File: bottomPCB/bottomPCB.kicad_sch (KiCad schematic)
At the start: 43 parts, among them J1 Conn_01x03_Pin, J2 Conn_02x03_Odd_Even, J3 Conn_01x02, J4 Conn_02x03_Odd_Even, U1 ESP32-WROOM-32, U2 XT30_horizontal, U3 XT30_horizontal, U8 LM1117IMPX-3_3_NOPB, U9 LM1117IMPX-3_3_NOPB

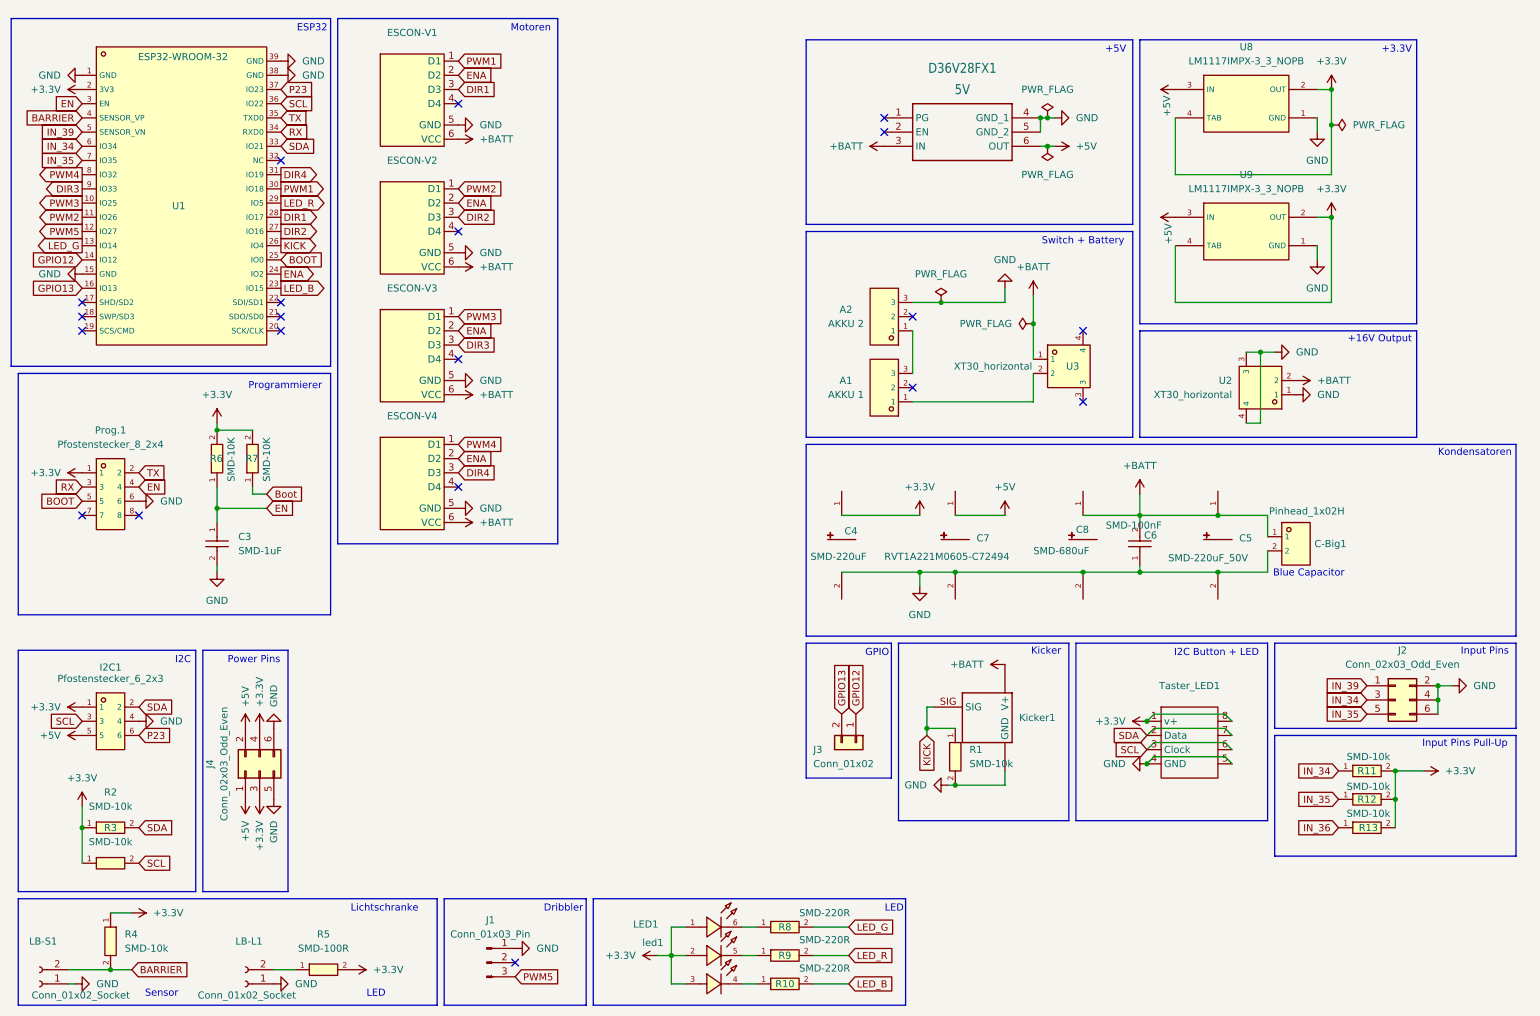
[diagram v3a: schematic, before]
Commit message: rearranged for vertical motor drivers
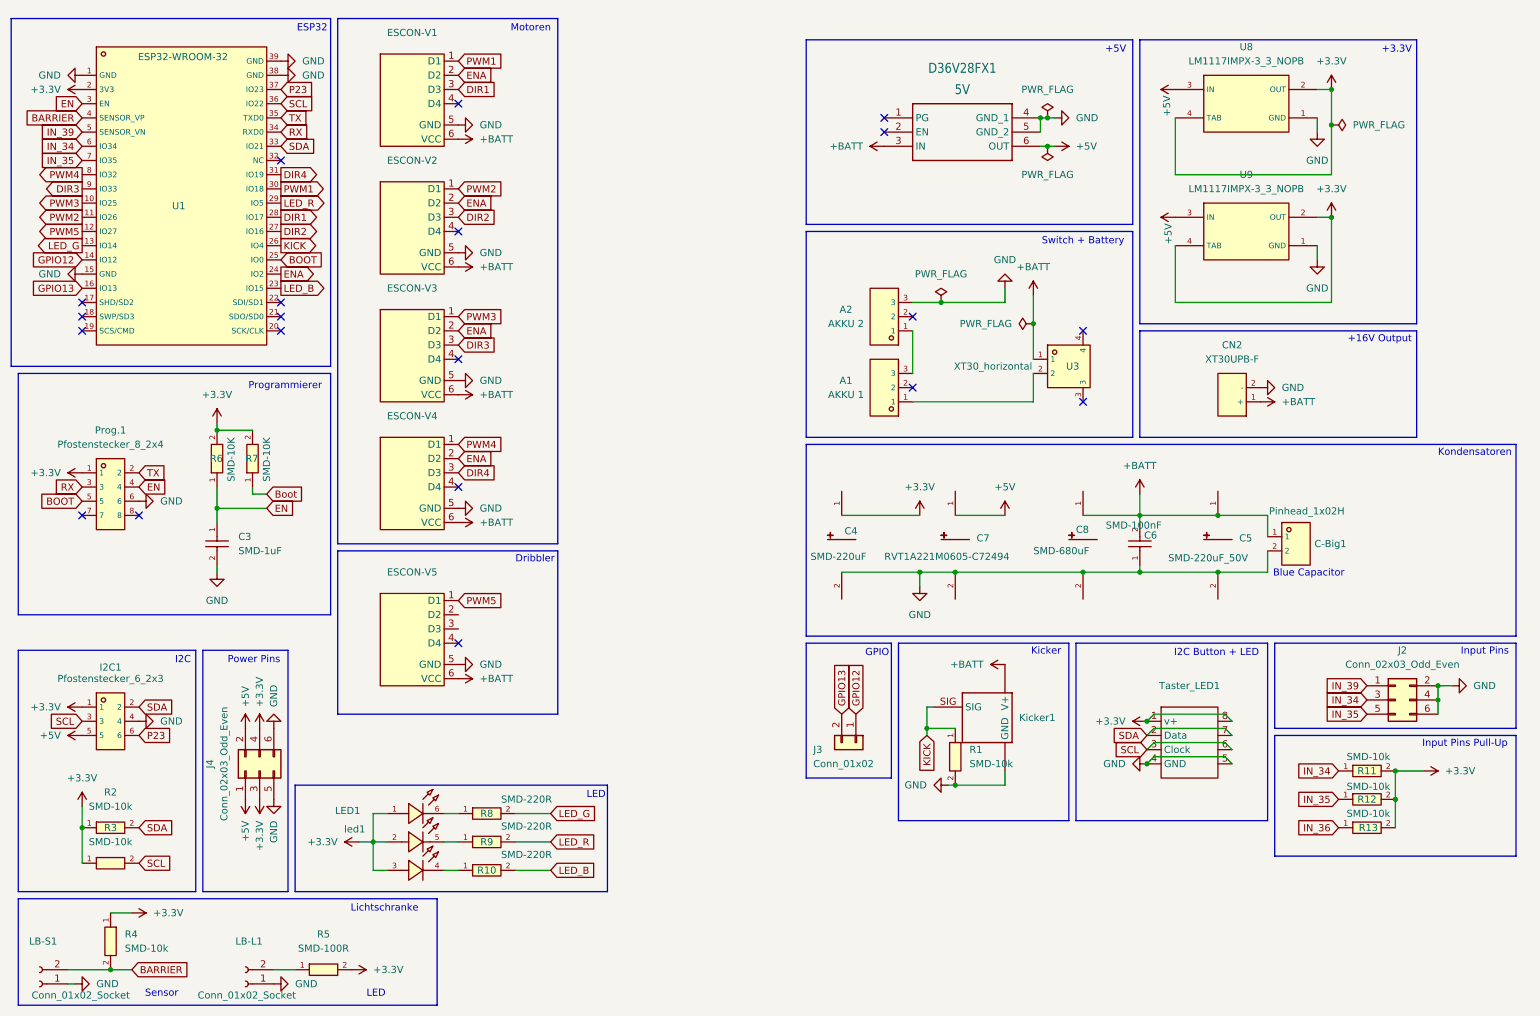
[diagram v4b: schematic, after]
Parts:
- removed J1: Conn_01x03_Pin, Connector_PinSocket_2.54mm:PinSocket_1x03_P2.54mm_Vertical, symbol Connector:Conn_01x03_Pin
- removed U2: XT30_horizontal, BohleBots:CONN-TH_XT30PW-M, symbol bohlebots.lib:XT30_horizontal
- added CN2: XT30UPB-F, BohleBots:CONN-TH_XT30UPB-F, symbol bohlebots.lib:XT30UPB-F
- added ESCON-V5: ~, sarcat:ESCON-V, symbol sarcat:ESCON-V
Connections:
- net +BATT: now also CN2.1 (+), ESCON-V5.6 (VCC)
- net GND: now also CN2.2 (-), ESCON-V5.5 (GND)
- net PWM5: now also ESCON-V5.1 (D1)
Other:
- moved on the sheet: LED1, R10, R8, R9

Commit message: added rules + changed layout
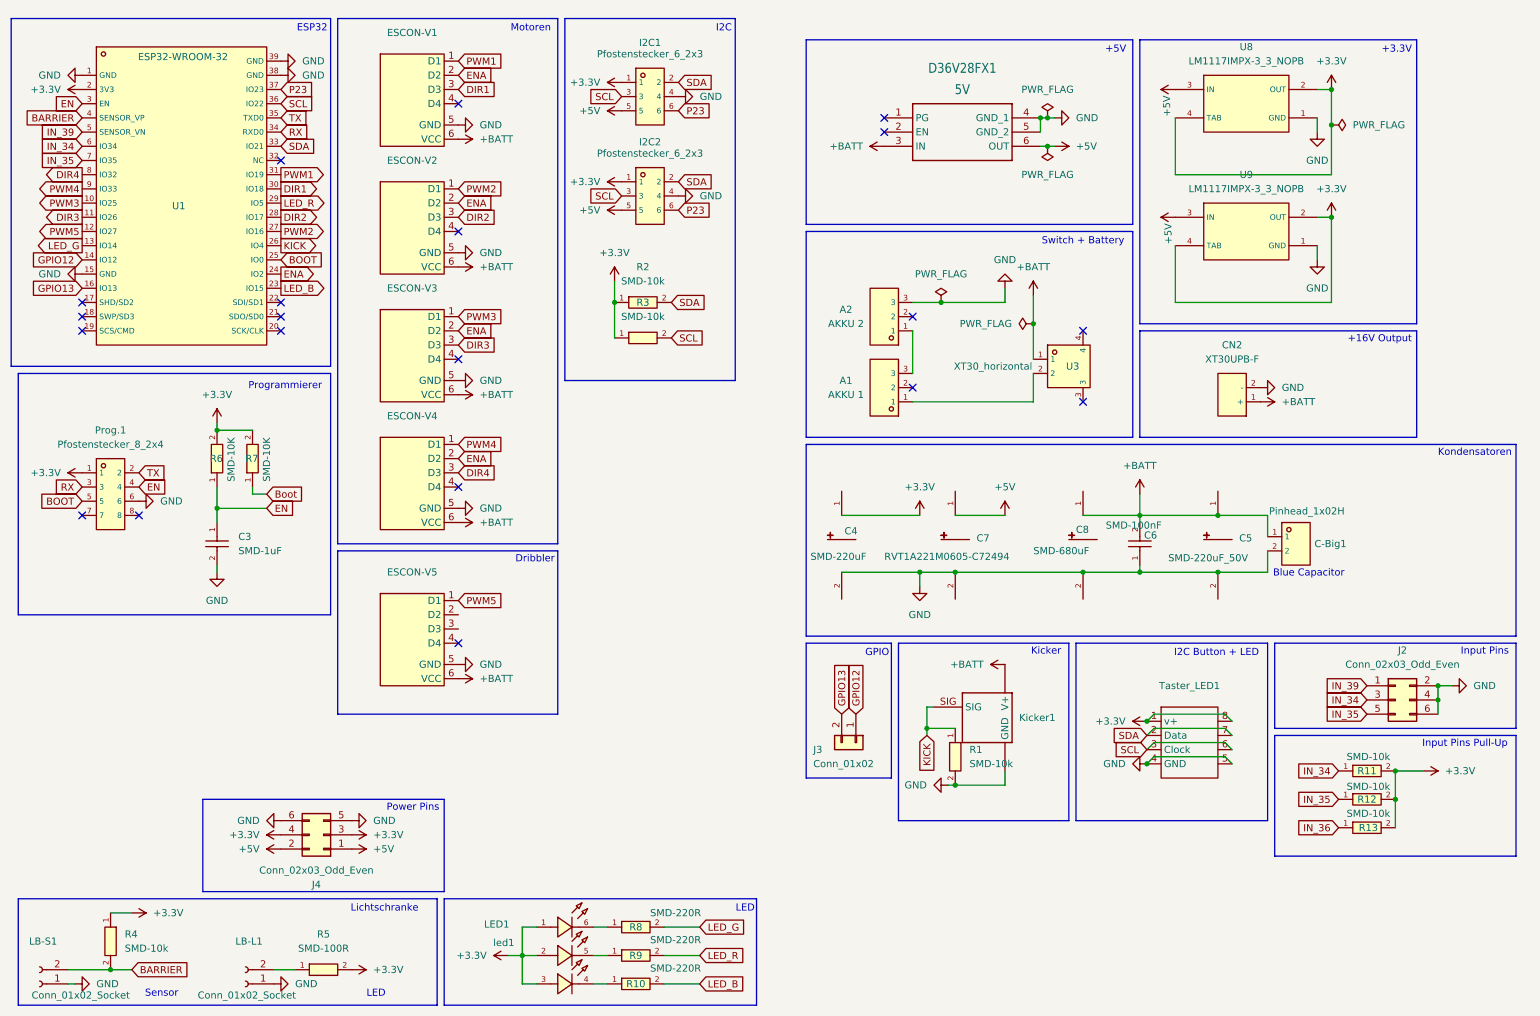
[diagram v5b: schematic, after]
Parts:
- added I2C2: Pfostenstecker_6_2x3, BohleBots:HDR-TH_6P-P2.54-V-F-R2-C3-S2.54-4, symbol bohlebots.lib:Pfostenstecker_6_2x3
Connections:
- net +3.3V: now also I2C2.1
- net +5V: now also I2C2.5
- net DIR1: now also U1.30 (IO18); no longer U1.28 (IO17)
- net DIR2: now also U1.28 (IO17); no longer U1.27 (IO16)
- net DIR3: now also U1.11 (IO26); no longer U1.9 (IO33)
- net DIR4: now also U1.8 (IO32); no longer U1.31 (IO19)
- net GND: now also I2C2.4
- net P23: now also I2C2.6
- net PWM1: now also U1.31 (IO19); no longer U1.30 (IO18)
- net PWM2: now also U1.27 (IO16); no longer U1.11 (IO26)
- net PWM4: now also U1.9 (IO33); no longer U1.8 (IO32)
- net SCL: now also I2C2.3
- net SDA: now also I2C2.2
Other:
- moved on the sheet: I2C1, J4, LED1, R10, R2, R3, R8, R9

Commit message: set traces
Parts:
- added H1, H2, H3, H4: MountingHole, BohleBots:MountingHole_4.3mm_M4, symbol bohlebots.lib:MountingHole
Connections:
- net Boot is gone; now on net BOOT: R7.1
- net IN_36 is gone; now on net IN_39: R13.1
- net +3.3V: now also ESCON-V5.2 (D2), ESCON-V5.3 (D3)
- net DIR2: now also U1.27 (IO16); no longer U1.28 (IO17)
- net DIR4: now also U1.9 (IO33); no longer U1.8 (IO32)
- net PWM2: now also U1.28 (IO17); no longer U1.27 (IO16)
- net PWM4: now also U1.8 (IO32); no longer U1.9 (IO33)

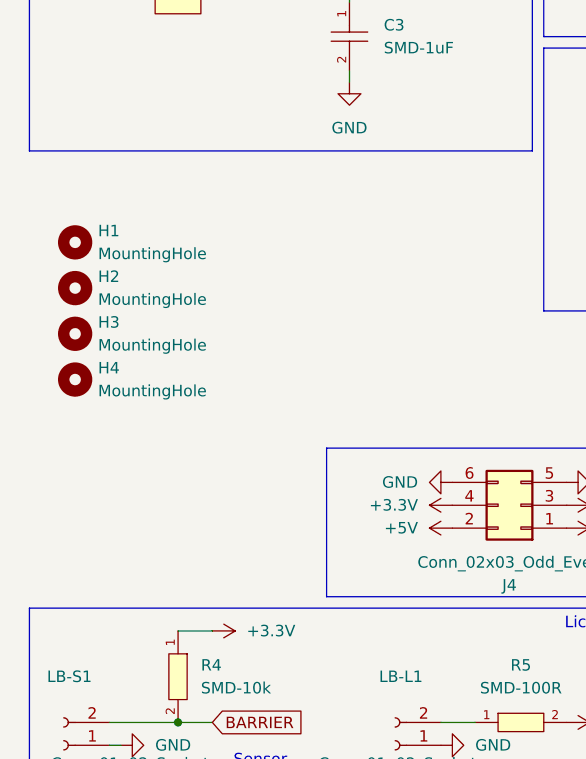
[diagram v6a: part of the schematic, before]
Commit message: Grounded Mounting Holes
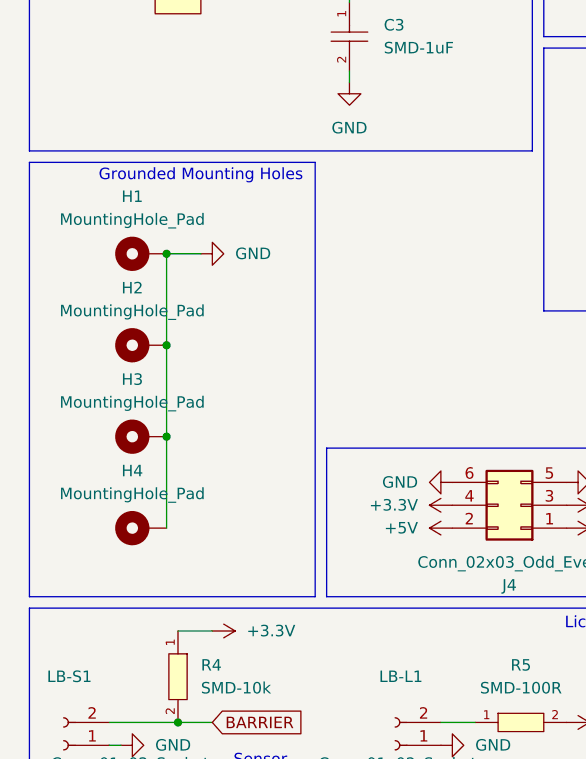
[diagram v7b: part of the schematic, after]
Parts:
- removed H1, H2, H3, H4: MountingHole, BohleBots:MountingHole_4.3mm_M4, symbol bohlebots.lib:MountingHole
- added H1, H2, H3, H4: MountingHole_Pad, MountingHole:MountingHole_4.3mm_M4_Pad, symbol Mechanical:MountingHole_Pad
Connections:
- net GND: now also H1.1, H2.1, H3.1, H4.1
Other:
- note added: "Grounded Mounting Holes"

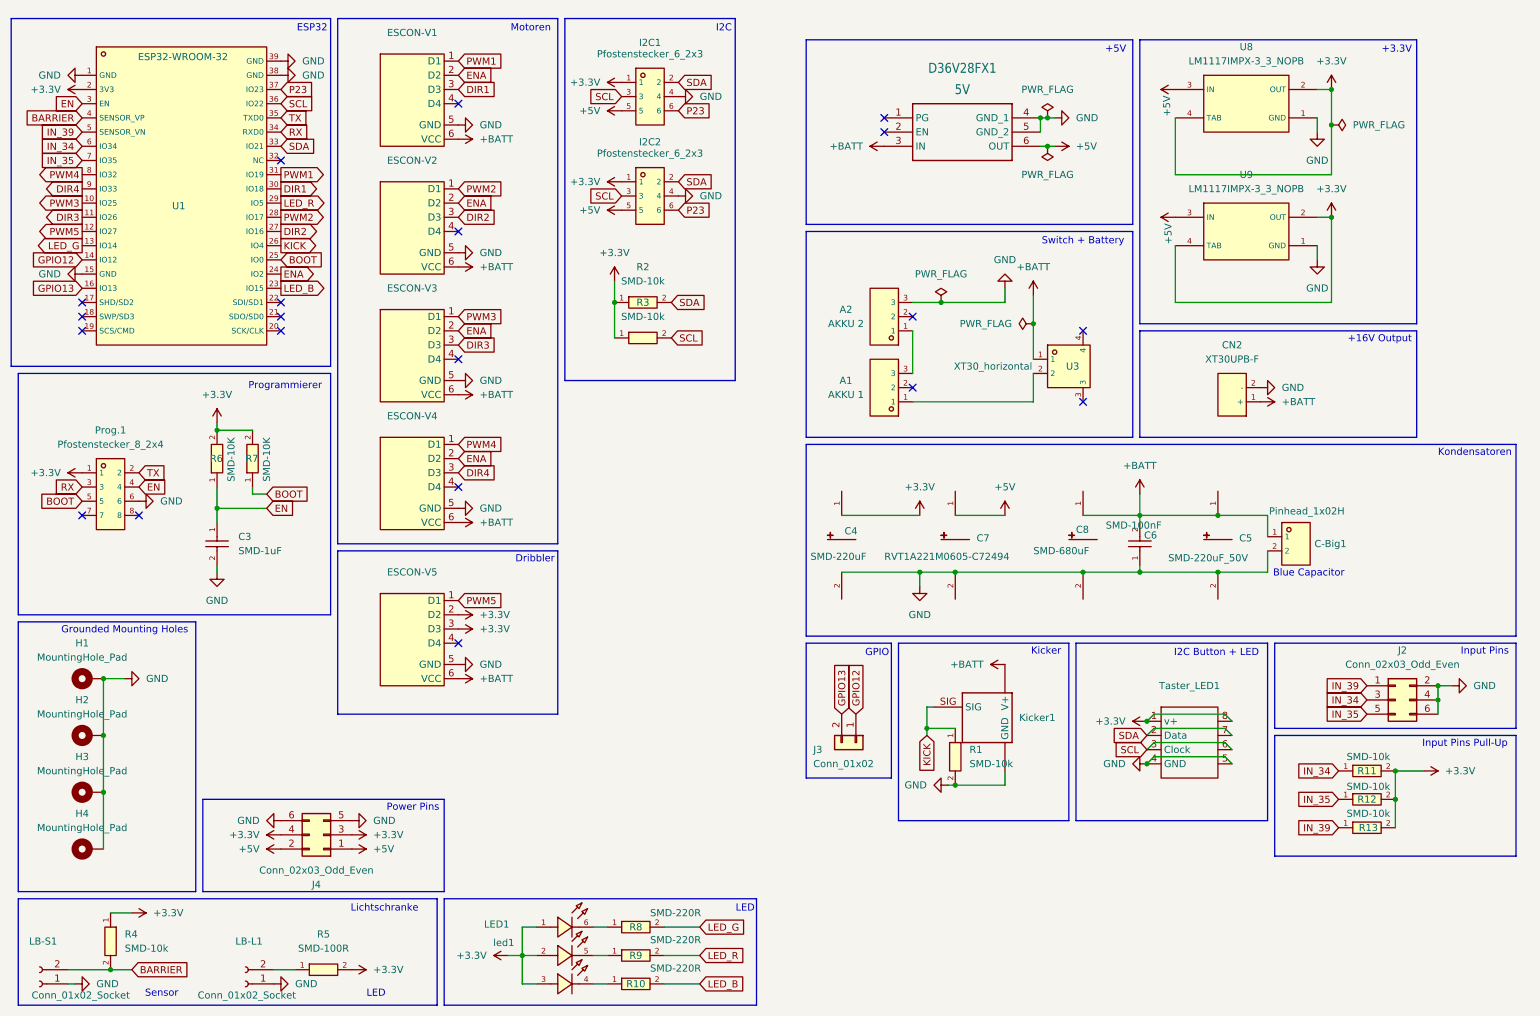
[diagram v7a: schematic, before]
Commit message: fixed erc errors
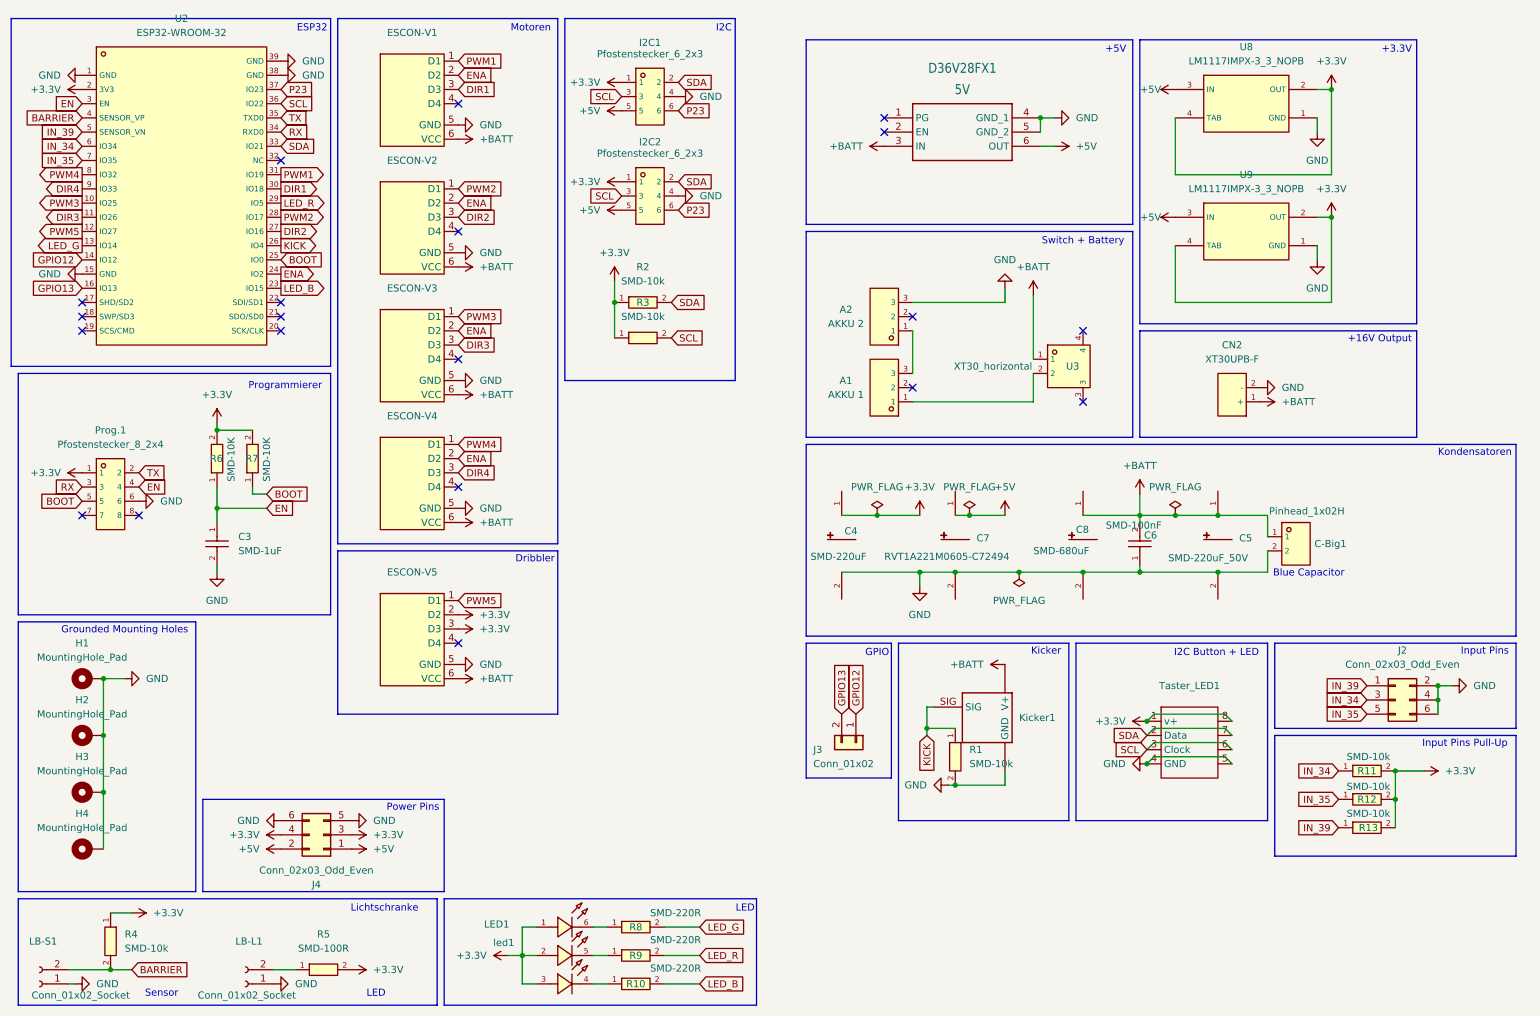
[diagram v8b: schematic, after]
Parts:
- removed U1: ESP32-WROOM-32, BohleBots:WIFIM-SMD_ESP32-WROOM-32-N4, symbol bohlebots.lib:ESP32-WROOM-32
- added U2: ESP32-WROOM-32, BohleBots:WIFIM-SMD_ESP32-WROOM-32-N4, symbol bohlebots.lib:ESP32-WROOM-32
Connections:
- net +3.3V: now also U2.2 (3V3)
- net BARRIER: now also U2.4 (SENSOR_VP)
- net BOOT: now also U2.25 (IO0)
- net DIR1: now also U2.30 (IO18)
- net DIR2: now also U2.27 (IO16)
- net DIR3: now also U2.11 (IO26)
- net DIR4: now also U2.9 (IO33)
- net EN: now also U2.3 (EN)
- net ENA: now also U2.24 (IO2)
- net GND: now also U2.1 (GND), U2.15 (GND), U2.38 (GND), U2.39 (GND)
- net GPIO12: now also U2.14 (IO12)
- net GPIO13: now also U2.16 (IO13)
- net IN_34: now also U2.6 (IO34)
- net IN_35: now also U2.7 (IO35)
- net IN_39: now also U2.5 (SENSOR_VN)
- net KICK: now also U2.26 (IO4)
- net LED_B: now also U2.23 (IO15)
- net LED_G: now also U2.13 (IO14)
- net LED_R: now also U2.29 (IO5)
- net P23: now also U2.37 (IO23)
- net PWM1: now also U2.31 (IO19)
- net PWM2: now also U2.28 (IO17)
- net PWM3: now also U2.10 (IO25)
- net PWM4: now also U2.8 (IO32)
- net PWM5: now also U2.12 (IO27)
- net RX: now also U2.34 (RXD0)
- net SCL: now also U2.36 (IO22)
- net SDA: now also U2.33 (IO21)
- net TX: now also U2.35 (TXD0)
